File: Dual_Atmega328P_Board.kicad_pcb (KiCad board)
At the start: 2 copper layers, 57 x 37.5 mm, 34 parts, among them IC1 ATmega328P-AU, IC2 ATmega328P-AU, J1 USB_B_Mini, J2 Conn_02x03_Odd_Even, J3 Conn_02x03_Odd_Even, J4 Conn_01x21, J5 Conn_01x21, SW1 SW_Push_DPDT, SW2 RESET, U1 FT232RL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

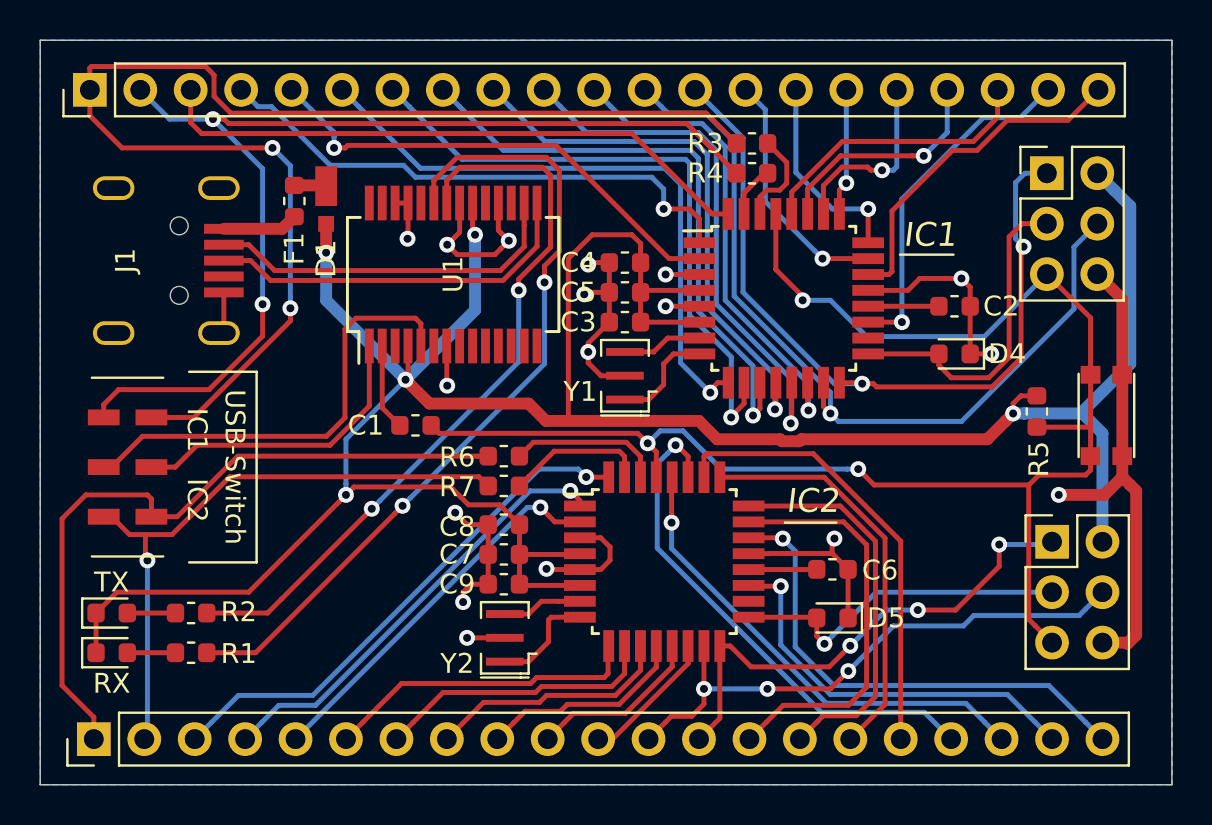
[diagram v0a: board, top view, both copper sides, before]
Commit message: Updated layout
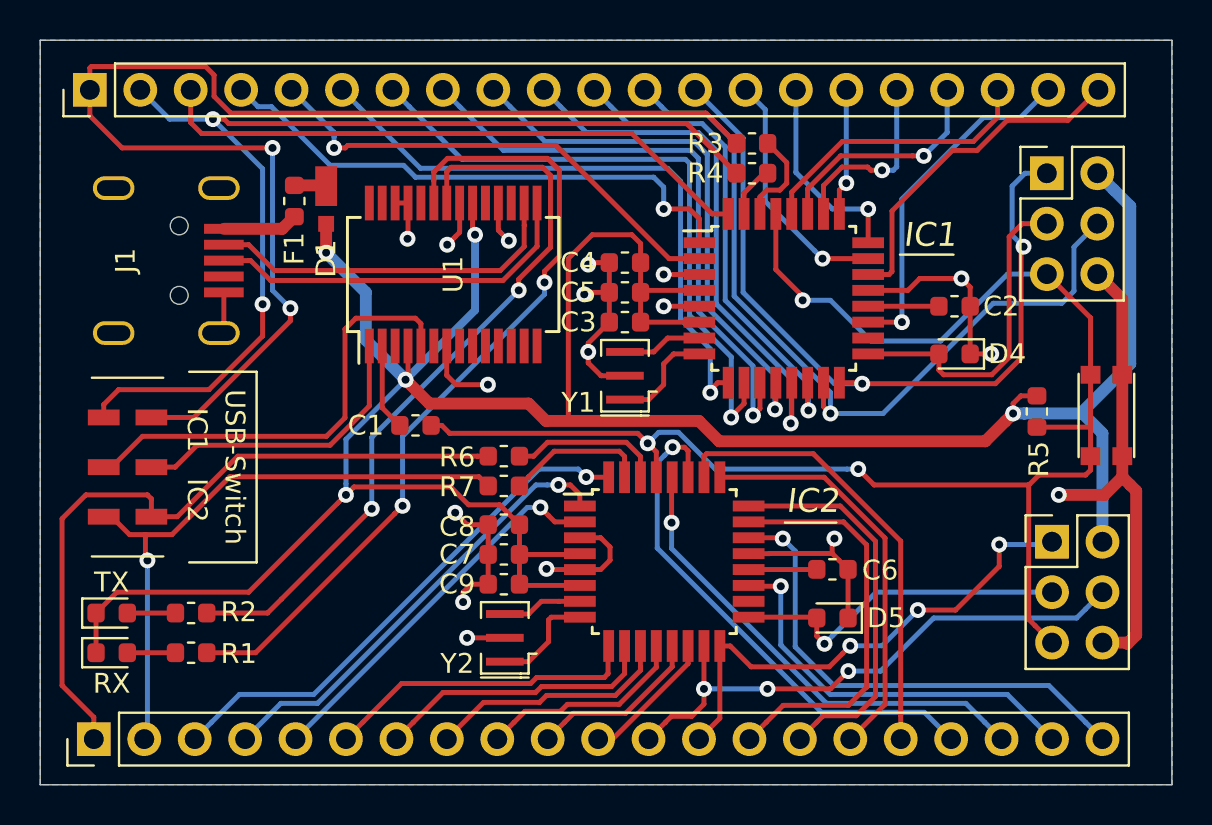
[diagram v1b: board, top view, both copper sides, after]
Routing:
- net GND: track 85.7 -> 83.8 mm
- net /D11_1: track 42.5 -> 41.7 mm

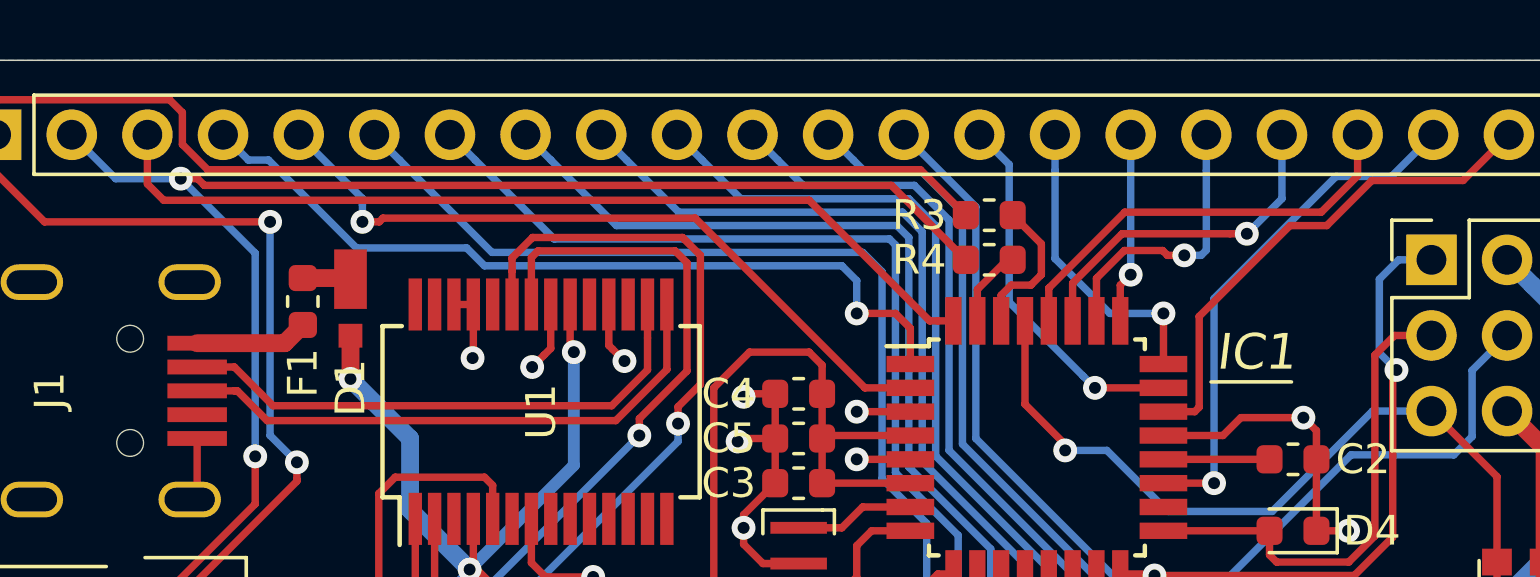
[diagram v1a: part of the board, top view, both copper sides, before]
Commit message: Updated layout
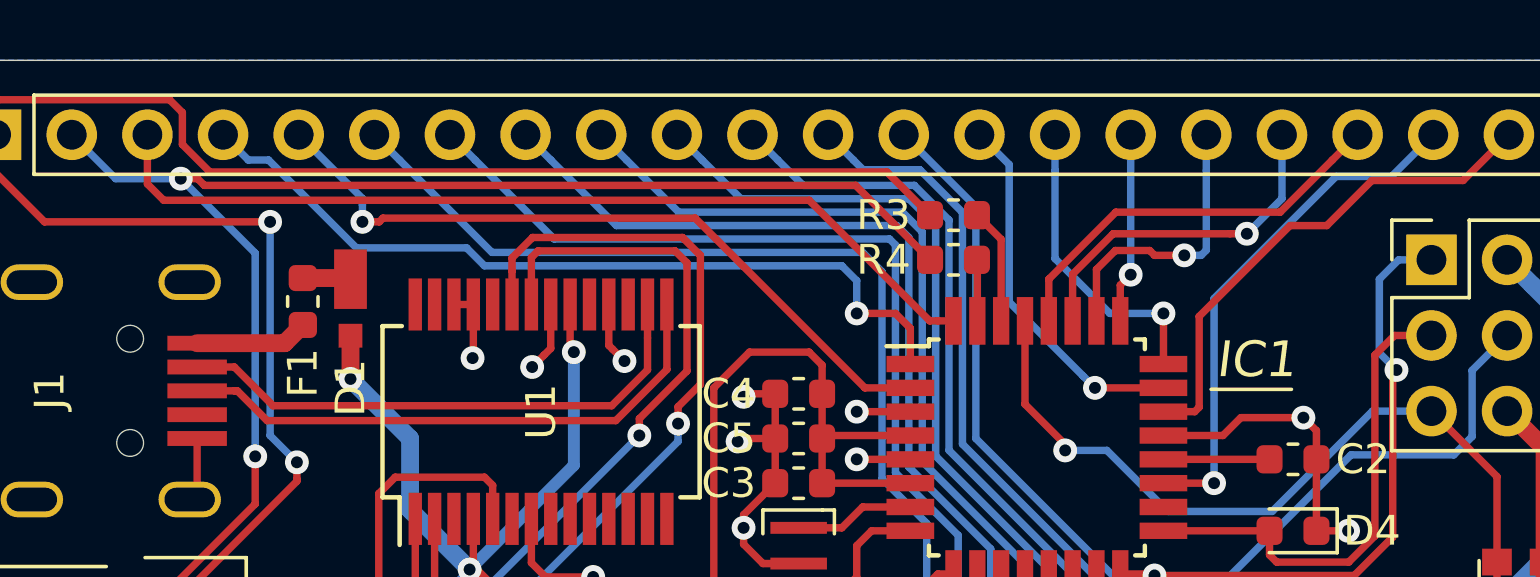
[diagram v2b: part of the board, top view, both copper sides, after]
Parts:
- moved R3 1.20 mm to (129.7, 32.7)
- moved R4 1.20 mm to (129.7, 34.2)
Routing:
- net /TX_1: track 53.9 -> 52.7 mm
- net /RX_1: track 65.2 -> 64.0 mm
- net /Atmega328P_1/D0_RX: track 4.85 -> 3.89 mm
- net /Atmega328P_1/D1_TX: track 2.70 -> 2.06 mm
- net /A5_1: track 14.4 -> 13.8 mm
